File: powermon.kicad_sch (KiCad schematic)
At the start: 27 parts, among them J1 2060-452/998-404, J2 2060-452/998-404, J3 2060-452/998-404, J5 2060-452/998-404, J6 2060-452/998-404, U1 PAC1953T-E_J6CX

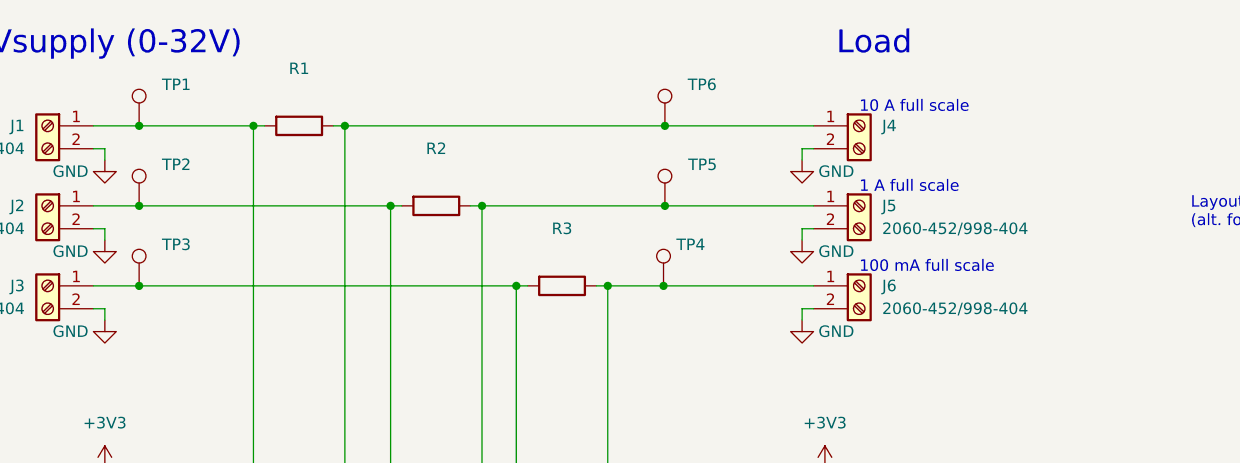
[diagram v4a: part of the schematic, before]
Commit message: Associate built-in footprints
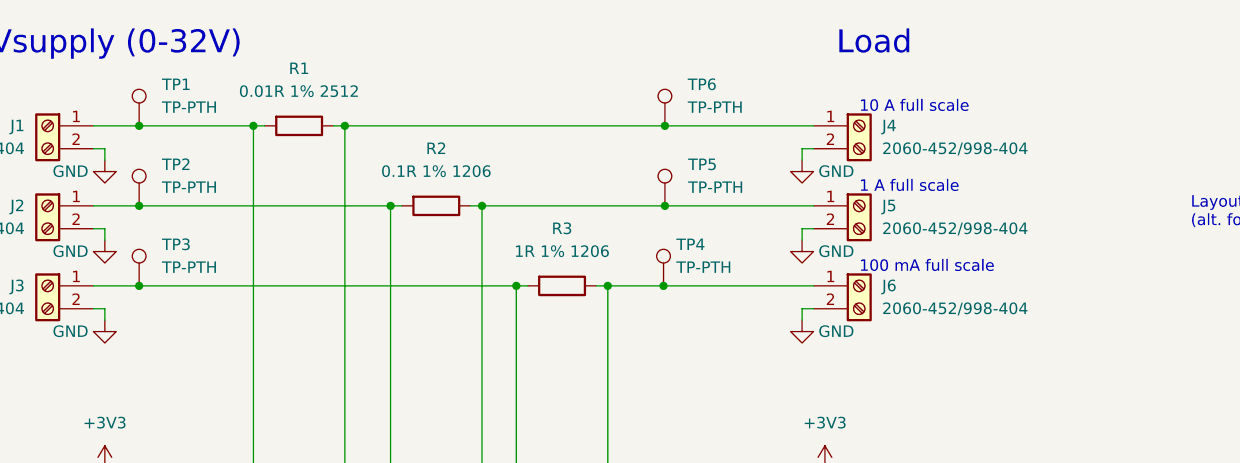
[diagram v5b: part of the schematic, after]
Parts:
- C1: footprint (none) -> Capacitor_SMD:C_0603_1608Metric
- C2: footprint (none) -> Capacitor_SMD:C_0402_1005Metric
- J4: value (none) -> 2060-452/998-404
- R1: value (none) -> 0.01R 1% 2512; footprint (none) -> Resistor_SMD:R_2512_6332Metric
- R2: value (none) -> 0.1R 1% 1206; footprint (none) -> Resistor_SMD:R_1206_3216Metric
- R3: value (none) -> 1R 1% 1206; footprint (none) -> Resistor_SMD:R_1206_3216Metric
- R4, R5, R6: footprint (none) -> Resistor_SMD:R_0402_1005Metric
- TP1, TP2, TP3, TP4, TP5, TP6: value (none) -> TP-PTH; footprint (none) -> TestPoint:TestPoint_THTPad_D4.0mm_Drill2.0mm
- TP10, TP11, TP12, TP7, TP8, TP9: footprint (none) -> TestPoint:TestPoint_THTPad_D4.0mm_Drill2.0mm
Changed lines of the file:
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@@
       (effects (font (size 1.27 1.27)) (justify left))
     )
-    (property "Footprint" "" (id 2) (at 197.612 97.79 90)
+    (property "Footprint" "Resistor_SMD:R_0402_1005Metric" (id 2) (at 197.612 97.79 90)
       (effects (font (size 1.27 1.27)) hide)
     )
@@
       (effects (font (size 1.27 1.27)) (justify left))
     )
-    (property "Footprint" "" (id 2) (at 187.452 97.79 90)
+    (property "Footprint" "Resistor_SMD:R_0402_1005Metric" (id 2) (at 187.452 97.79 90)
       (effects (font (size 1.27 1.27)) hide)
     )
@@
       (effects (font (size 1.27 1.27)) (justify left))
     )
-    (property "Value" "" (id 1) (at 115.57 65.2779 0)
-      (effects (font (size 1.27 1.27)) (justify left))
-    )
-    (property "Footprint" "" (id 2) (at 118.11 67.31 0)
+    (property "Value" "TP-PTH" (id 1) (at 115.57 65.2779 0)
+      (effects (font (size 1.27 1.27)) (justify left))
+    )
+    (property "Footprint" "TestPoint:TestPoint_THTPad_D4.0mm_Drill2.0mm" (id 2) (at 118.11 67.31 0)
       (effects (font (size 1.27 1.27)) hide)
     )
@@
       (effects (font (size 1.27 1.27)) (justify left))
     )
-    (property "Footprint" "" (id 2) (at 262.89 77.47 0)
+    (property "Footprint" "TestPoint:TestPoint_THTPad_D4.0mm_Drill2.0mm" (id 2) (at 262.89 77.47 0)
       (effects (font (size 1.27 1.27)) hide)
     )
@@
       (effects (font (size 1.27 1.27)) (justify left))
     )
-    (property "Footprint" "" (id 2) (at 65.7352 100.33 0)
+    (property "Footprint" "Capacitor_SMD:C_0603_1608Metric" (id 2) (at 65.7352 100.33 0)
       (effects (font (size 1.27 1.27)) hide)
     )
@@
       (effects (font (size 1.27 1.27)) (justify left))
     )
-    (property "Footprint" "" (id 2) (at 251.46 77.47 0)
+    (property "Footprint" "TestPoint:TestPoint_THTPad_D4.0mm_Drill2.0mm" (id 2) (at 251.46 77.47 0)
       (effects (font (size 1.27 1.27)) hide)
     )
@@
       (effects (font (size 1.27 1.27)) (justify left))
     )
-    (property "Footprint" "" (id 2) (at 262.89 86.36 0)
+    (property "Footprint" "TestPoint:TestPoint_THTPad_D4.0mm_Drill2.0mm" (id 2) (at 262.89 86.36 0)
       (effects (font (size 1.27 1.27)) hide)
     )
@@
     (in_bom yes) (on_board yes) (fields_autoplaced)
     (property "Reference" "R2" (id 0) (at 146.05 52.07 90))
-    (property "Value" "" (id 1) (at 146.05 54.61 90))
-    (property "Footprint" "" (id 2) (at 146.05 56.642 90)
+    (property "Value" "0.1R 1% 1206" (id 1) (at 146.05 54.61 90))
+    (property "Footprint" "Resistor_SMD:R_1206_3216Metric" (id 2) (at 146.05 56.642 90)
       (effects (font (size 1.27 1.27)) hide)
     )
@@
       (effects (font (size 1.27 1.27)) (justify left))
     )
-    (property "Value" "" (id 1) (at 195.58 52.0699 0)
+    (property "Value" "2060-452/998-404" (id 1) (at 195.58 52.0699 0)
       (effects (font (size 1.27 1.27)) (justify left))
     )
@@
     (in_bom yes) (on_board yes) (fields_autoplaced)
     (property "Reference" "R3" (id 0) (at 160.02 60.96 90))
-    (property "Value" "" (id 1) (at 160.02 63.5 90))
-    (property "Footprint" "" (id 2) (at 160.02 65.532 90)
+    (property "Value" "1R 1% 1206" (id 1) (at 160.02 63.5 90))
+    (property "Footprint" "Resistor_SMD:R_1206_3216Metric" (id 2) (at 160.02 65.532 90)
       (effects (font (size 1.27 1.27)) hide)
     )
@@
       (effects (font (size 1.27 1.27)) (justify left))
     )
-    (property "Value" "" (id 1) (at 174.0345 56.3879 0)
-      (effects (font (size 1.27 1.27)) (justify left))
-    )
-    (property "Footprint" "" (id 2) (at 176.53 58.42 0)
+    (property "Value" "TP-PTH" (id 1) (at 174.0345 56.3879 0)
+      (effects (font (size 1.27 1.27)) (justify left))
+    )
+    (property "Footprint" "TestPoint:TestPoint_THTPad_D4.0mm_Drill2.0mm" (id 2) (at 176.53 58.42 0)
       (effects (font (size 1.27 1.27)) hide)
     )
@@
       (effects (font (size 1.27 1.27)) (justify left))
     )
-    (property "Footprint" "" (id 2) (at 78.4352 100.33 0)
+    (property "Footprint" "Capacitor_SMD:C_0402_1005Metric" (id 2) (at 78.4352 100.33 0)
       (effects (font (size 1.27 1.27)) hide)
     )
@@
       (effects (font (size 1.27 1.27)) (justify left))
     )
-    (property "Footprint" "" (id 2) (at 251.46 68.58 0)
+    (property "Footprint" "TestPoint:TestPoint_THTPad_D4.0mm_Drill2.0mm" (id 2) (at 251.46 68.58 0)
       (effects (font (size 1.27 1.27)) hide)
     )
@@
       (effects (font (size 1.27 1.27)) (justify left))
     )
-    (property "Value" "" (id 1) (at 172.72 65.2779 0)
-      (effects (font (size 1.27 1.27)) (justify left))
-    )
-    (property "Footprint" "" (id 2) (at 176.3762 67.31 0)
+    (property "Value" "TP-PTH" (id 1) (at 172.72 65.2779 0)
+      (effects (font (size 1.27 1.27)) (justify left))
+    )
+    (property "Footprint" "TestPoint:TestPoint_THTPad_D4.0mm_Drill2.0mm" (id 2) (at 176.3762 67.31 0)
       (effects (font (size 1.27 1.27)) hide)
     )
@@
       (effects (font (size 1.27 1.27)) (justify left))
     )
-    (property "Value" "" (id 1) (at 115.57 47.4979 0)
-      (effects (font (size 1.27 1.27)) (justify left))
-    )
-    (property "Footprint" "" (id 2) (at 118.11 49.53 0)
+    (property "Value" "TP-PTH" (id 1) (at 115.57 47.4979 0)
+      (effects (font (size 1.27 1.27)) (justify left))
+    )
+    (property "Footprint" "TestPoint:TestPoint_THTPad_D4.0mm_Drill2.0mm" (id 2) (at 118.11 49.53 0)
       (effects (font (size 1.27 1.27)) hide)
     )
@@
       (effects (font (size 1.27 1.27)) (justify left))
     )
-    (property "Footprint" "" (id 2) (at 262.89 68.58 0)
+    (property "Footprint" "TestPoint:TestPoint_THTPad_D4.0mm_Drill2.0mm" (id 2) (at 262.89 68.58 0)
       (effects (font (size 1.27 1.27)) hide)
     )
@@
       (effects (font (size 1.27 1.27)) (justify left))
     )
-    (property "Footprint" "" (id 2) (at 207.772 97.79 90)
+    (property "Footprint" "Resistor_SMD:R_0402_1005Metric" (id 2) (at 207.772 97.79 90)
       (effects (font (size 1.27 1.27)) hide)
     )
@@
       (effects (font (size 1.27 1.27)) (justify left))
     )
-    (property "Footprint" "" (id 2) (at 251.46 86.36 0)
+    (property "Footprint" "TestPoint:TestPoint_THTPad_D4.0mm_Drill2.0mm" (id 2) (at 251.46 86.36 0)
       (effects (font (size 1.27 1.27)) hide)
     )
@@
       (effects (font (size 1.27 1.27)) (justify left))
     )
-    (property "Value" "" (id 1) (at 115.57 56.3879 0)
-      (effects (font (size 1.27 1.27)) (justify left))
-    )
-    (property "Footprint" "" (id 2) (at 118.11 58.42 0)
+    (property "Value" "TP-PTH" (id 1) (at 115.57 56.3879 0)
+      (effects (font (size 1.27 1.27)) (justify left))
+    )
+    (property "Footprint" "TestPoint:TestPoint_THTPad_D4.0mm_Drill2.0mm" (id 2) (at 118.11 58.42 0)
       (effects (font (size 1.27 1.27)) hide)
     )
@@
     (in_bom yes) (on_board yes) (fields_autoplaced)
     (property "Reference" "R1" (id 0) (at 130.81 43.18 90))
-    (property "Value" "" (id 1) (at 130.81 45.72 90))
-    (property "Footprint" "" (id 2) (at 130.81 47.752 90)
+    (property "Value" "0.01R 1% 2512" (id 1) (at 130.81 45.72 90))
+    (property "Footprint" "Resistor_SMD:R_2512_6332Metric" (id 2) (at 130.81 47.752 90)
       (effects (font (size 1.27 1.27)) hide)
     )
@@
       (effects (font (size 1.27 1.27)) (justify left))
     )
-    (property "Value" "" (id 1) (at 173.99 47.4979 0)
-      (effects (font (size 1.27 1.27)) (justify left))
-    )
-    (property "Footprint" "" (id 2) (at 176.53 49.53 0)
-      (effects (font (size 1.27 1.27)) hide)
-    )
+    (property "Value" "TP-PTH" (id 1) (at 173.99 47.4979 0)
+      (effects (font (size 1.27 1.27)) (justify left))
+    )
+    (property "Footprint" "TestPoint:TestPoint_THTPad_D4.0mm_Drill2.0mm" (id 2) (at 176.53 49.53 0)
+      (effects (font (size 1.27 1.27)) hide)
+    )

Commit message: Add part number fields in schematic
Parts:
- C1, C2, R4, R5, R6: MfgPartNo (none) -> GENERIC
- J1, J2, J3, J4, J5, J6: Manufacturer (none) -> Wago; MfgPartNo (none) -> 2060-452/998-404; Vendor (none) -> Digi-Key; VendorPartNo (none) -> 2946-2060-452/998-404CT-ND
- R1: Manufacturer (none) -> YAGEO; MfgPartNo (none) -> PA2512FKE7W0R01E; Vendor (none) -> Digi-Key; VendorPartNo (none) -> YAG6093CT-ND
- R2: Manufacturer (none) -> YAGEO; MfgPartNo (none) -> PE1206FRM7W0R1L; Vendor (none) -> Digi-Key; VendorPartNo (none) -> YAG6112CT-ND
- R3: Manufacturer (none) -> YAGEO; MfgPartNo (none) -> RC1206FR-131RL; Vendor (none) -> Digi-Key; VendorPartNo (none) -> 13-RC1206FR-131RLCT-ND
- U1: Manufacturer (none) -> Microchip; MfgPartNo (none) -> PAC1953T-E/J6CX; Vendor (none) -> Digi-Key; VendorPartNo (none) -> 150-PAC1953T-E/J6CXCT-ND

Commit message: PAC1953 footprint
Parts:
- U1: footprint (none) -> toast:BGA16NP50_4X4_222X217X67B32N
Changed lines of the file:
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@@
     (property "Reference" "U1" (id 0) (at 143.51 124.46 0))
     (property "Value" "PAC1953T-E_J6CX" (id 1) (at 143.51 127 0))
-    (property "Footprint" "" (id 2) (at 133.35 91.44 0)
+    (property "Footprint" "toast:BGA16NP50_4X4_222X217X67B32N" (id 2) (at 133.35 91.44 0)
       (effects (font (size 1.27 1.27)) hide)
     )

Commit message: Stencil alignment holes and WAGO 2060-452 footprint
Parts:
- J1, J2, J3, J4, J5, J6: footprint (none) -> toast:WAGO_2060-452_998-404; symbol Connector:Screw_Terminal_01x02 -> ik:WAGO_2060-452-998-404
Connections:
- net GND: now also J1.4 (Pin_4), J2.4 (Pin_4), J3.4 (Pin_4), J4.4 (Pin_4), J5.4 (Pin_4), J6.4 (Pin_4)
- net at J2.1 (Pin_1), R2.2, TP2.1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: now also J2.3 (Pin_3)
- net at J3.1 (Pin_1), R3.2, TP3.1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: now also J3.3 (Pin_3)
- net at J5.1 (Pin_1), R2.1, TP5.1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: now also J5.3 (Pin_3)
- net at J6.1 (Pin_1), R3.1, TP4.1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: now also J6.3 (Pin_3)
- net at J4.1 (Pin_1), R1.1, TP6.1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: now also J4.3 (Pin_3)
- net at J1.1 (Pin_1), R1.2, TP1.1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: now also J1.3 (Pin_3)
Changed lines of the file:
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@@
     (pin "1")
   )
-  (symbol (lib_id "Connector:Screw_Terminal_01x02") (at 102.87 58.42 0) (mirror y) (unit 1)
+  (symbol (lib_id "ik:WAGO_2060-452-998-404") (at 102.87 58.42 0) (mirror y) (unit 1)
     (in_bom yes) (on_board yes) (fields_autoplaced)
     (property "Reference" "J2" (id 0) (at 100.33 58.4199 0)
@@
       (effects (font (size 1.27 1.27)) (justify left))
     )
-    (property "Footprint" "" (id 2) (at 102.87 58.42 0)
+    (property "Footprint" "toast:WAGO_2060-452_998-404" (id 2) (at 102.87 58.42 0)
       (effects (font (size 1.27 1.27)) hide)
     )
@@
       (effects (font (size 1.27 1.27)) (justify left) hide)
     )
+    (pin "3")
+    (pin "4")
     (pin "1")
     (pin "2")
@@
     (pin "2")
   )
-  (symbol (lib_id "Connector:Screw_Terminal_01x02") (at 193.04 67.31 0) (unit 1)
+  (symbol (lib_id "ik:WAGO_2060-452-998-404") (at 193.04 67.31 0) (unit 1)
     (in_bom yes) (on_board yes) (fields_autoplaced)
     (property "Reference" "J6" (id 0) (at 195.58 67.3099 0)
@@
       (effects (font (size 1.27 1.27)) (justify left))
     )
-    (property "Footprint" "" (id 2) (at 193.04 67.31 0)
+    (property "Footprint" "toast:WAGO_2060-452_998-404" (id 2) (at 193.04 67.31 0)
       (effects (font (size 1.27 1.27)) hide)
     )
@@
       (effects (font (size 1.27 1.27)) (justify left) hide)
     )
+    (pin "3")
+    (pin "4")
     (pin "1")
     (pin "2")
@@
     (pin "1")
   )
-  (symbol (lib_id "Connector:Screw_Terminal_01x02") (at 193.04 49.53 0) (unit 1)
+  (symbol (lib_id "ik:WAGO_2060-452-998-404") (at 193.04 49.53 0) (unit 1)
     (in_bom yes) (on_board yes) (fields_autoplaced)
     (property "Reference" "J4" (id 0) (at 195.58 49.5299 0)
@@
       (effects (font (size 1.27 1.27)) (justify left))
     )
-    (property "Footprint" "" (id 2) (at 193.04 49.53 0)
+    (property "Footprint" "toast:WAGO_2060-452_998-404" (id 2) (at 193.04 49.53 0)
       (effects (font (size 1.27 1.27)) hide)
     )
@@
       (effects (font (size 1.27 1.27)) (justify left) hide)
     )
+    (pin "3")
+    (pin "4")
     (pin "1")
     (pin "2")
@@
     (pin "1")
   )
-  (symbol (lib_id "Connector:Screw_Terminal_01x02") (at 102.87 67.31 0) (mirror y) (unit 1)
+  (symbol (lib_id "ik:WAGO_2060-452-998-404") (at 102.87 67.31 0) (mirror y) (unit 1)
     (in_bom yes) (on_board yes) (fields_autoplaced)
     (property "Reference" "J3" (id 0) (at 100.33 67.3099 0)
@@
       (effects (font (size 1.27 1.27)) (justify left))
     )
-    (property "Footprint" "" (id 2) (at 102.87 67.31 0)
+    (property "Footprint" "toast:WAGO_2060-452_998-404" (id 2) (at 102.87 67.31 0)
       (effects (font (size 1.27 1.27)) hide)
     )
@@
       (effects (font (size 1.27 1.27)) (justify left) hide)
     )
+    (pin "3")
+    (pin "4")
     (pin "1")
     (pin "2")
@@
     (pin "1")
   )
-  (symbol (lib_id "Connector:Screw_Terminal_01x02") (at 102.87 49.53 0) (mirror y) (unit 1)
+  (symbol (lib_id "ik:WAGO_2060-452-998-404") (at 102.87 49.53 0) (mirror y) (unit 1)
     (in_bom yes) (on_board yes) (fields_autoplaced)
     (property "Reference" "J1" (id 0) (at 100.33 49.5299 0)
@@
       (effects (font (size 1.27 1.27)) (justify left))
     )
-    (property "Footprint" "" (id 2) (at 102.87 49.53 0)
+    (property "Footprint" "toast:WAGO_2060-452_998-404" (id 2) (at 102.87 49.53 0)
       (effects (font (size 1.27 1.27)) hide)
     )
@@
       (effects (font (size 1.27 1.27)) (justify left) hide)
     )
-    (pin "1")
-    (pin "2")
-  )
-  (symbol (lib_id "Connector:Screw_Terminal_01x02") (at 193.04 58.42 0) (unit 1)
+    (pin "3")
+    (pin "4")
+    (pin "1")
+    (pin "2")
+  )
+  (symbol (lib_id "ik:WAGO_2060-452-998-404") (at 193.04 58.42 0) (unit 1)
     (in_bom yes) (on_board yes) (fields_autoplaced)
     (property "Reference" "J5" (id 0) (at 195.58 58.4199 0)
@@
       (effects (font (size 1.27 1.27)) (justify left))
     )
-    (property "Footprint" "" (id 2) (at 193.04 58.42 0)
+    (property "Footprint" "toast:WAGO_2060-452_998-404" (id 2) (at 193.04 58.42 0)
       (effects (font (size 1.27 1.27)) hide)
     )
@@
       (effects (font (size 1.27 1.27)) (justify left) hide)
     )
-    (pin "1")
-    (pin "2")
+    (pin "3")
+    (pin "4")
+    (pin "1")
+    (pin "2")
